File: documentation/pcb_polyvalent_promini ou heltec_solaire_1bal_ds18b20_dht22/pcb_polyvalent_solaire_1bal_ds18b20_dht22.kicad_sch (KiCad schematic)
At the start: 19 parts, among them J1 Conn_01x12, J10 Conn_01x08, J11 Conn_01x05, J12 Conn_01x02, J13 Conn_01x02, J14 Conn_01x02, J15 Conn_01x03, J2 Conn_01x12, J3 Conn_01x15, J4 Conn_01x15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

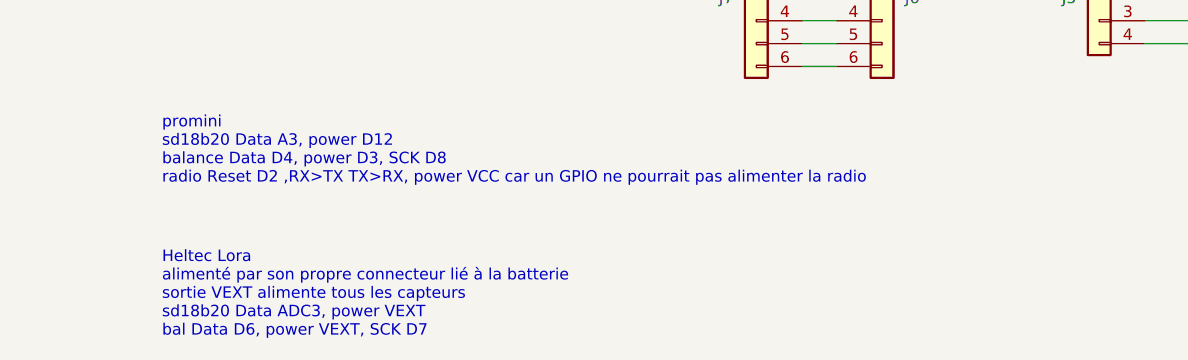
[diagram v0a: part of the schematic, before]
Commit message: changement commentaire dans schéma
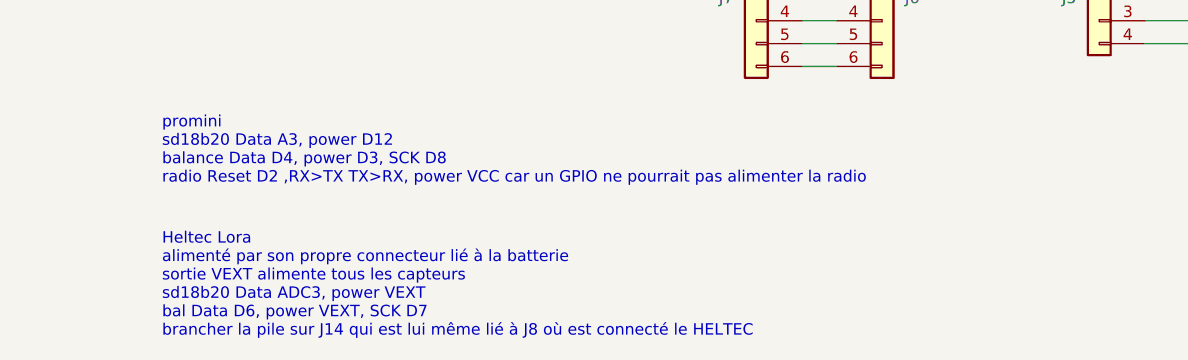
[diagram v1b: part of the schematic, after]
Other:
- note added: "Heltec Lora alimenté par son propre connecteur lié à la batterie sortie VEXT alimente tous les capteurs sd18b20 Data ADC3, power VEXT bal Data D6, power VEXT, SCK D7 brancher la pile sur J14 qui est lui même lié à J8 où est connecté le HELTEC"
- note removed: "Heltec Lora alimenté par son propre connecteur lié à la batterie sortie VEXT alimente tous les capteurs sd18b20 Data ADC3, power VEXT bal Data D6, power VEXT, SCK D7"
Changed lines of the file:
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@@
     (effects (font (size 1.27 1.27)) (justify left bottom))
   )
-  (text "Heltec Lora\nalimenté par son propre connecteur lié à la batterie\nsortie VEXT alimente tous les capteurs\nsd18b20 Data ADC3, power VEXT\nbal Data D6, power VEXT, SCK D7\n\n\n"
+  (text "Heltec Lora\nalimenté par son propre connecteur lié à la batterie\nsortie VEXT alimente tous les capteurs\nsd18b20 Data ADC3, power VEXT\nbal Data D6, power VEXT, SCK D7\nbrancher la pile sur J14 qui est lui même lié à J8 où est connecté le HELTEC\n\n\n"
     (at 45.72 180.34 0)
     (effects (font (size 1.27 1.27)) (justify left bottom))
